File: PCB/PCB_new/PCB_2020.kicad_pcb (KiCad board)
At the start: 2 copper layers, 102.2 x 94.5 mm, 28 parts, among them IC1 LM358N, Q1 220mA/50V/3.5Ω, Q2 100V/17A, Q3 100V/17A, Q4 100V/17A, Q5 100V/17A, Q6 100V/17A, U1 TI_CONN

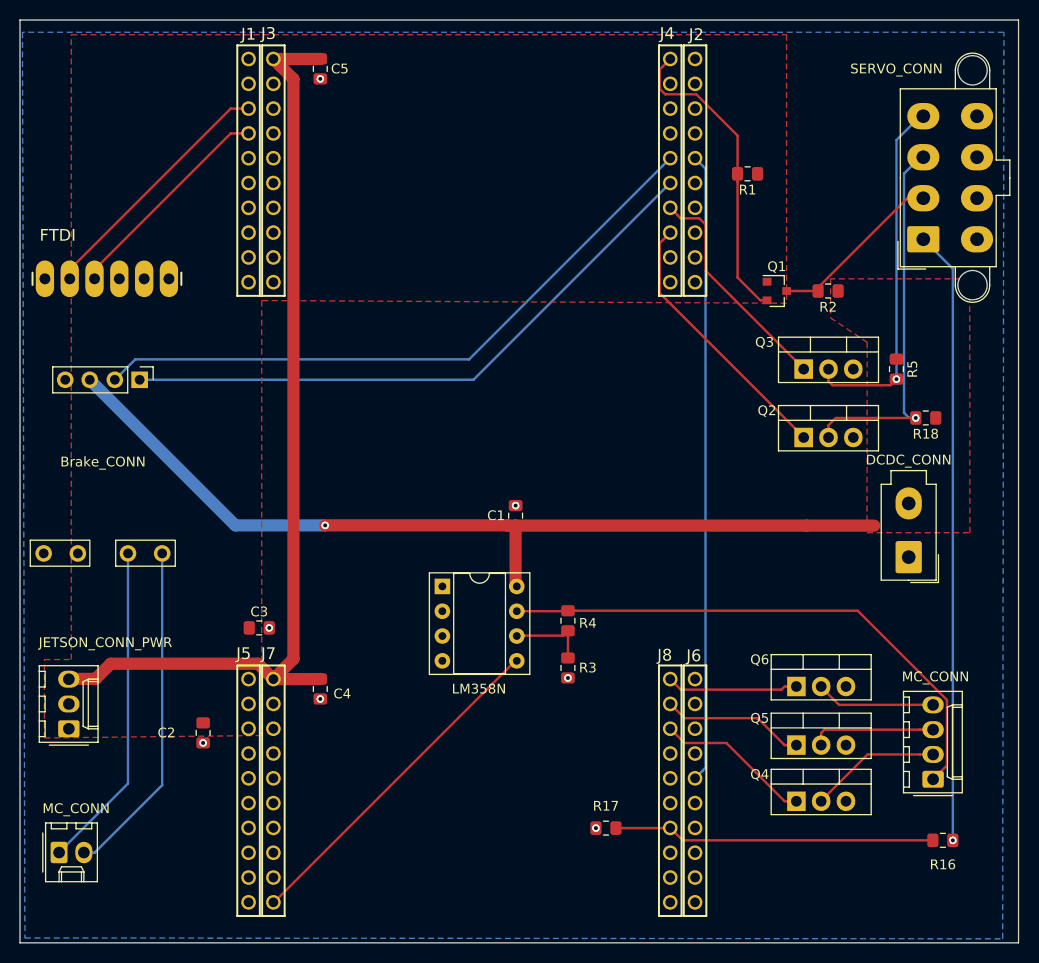
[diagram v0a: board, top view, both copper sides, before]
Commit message: fixed connector notation error
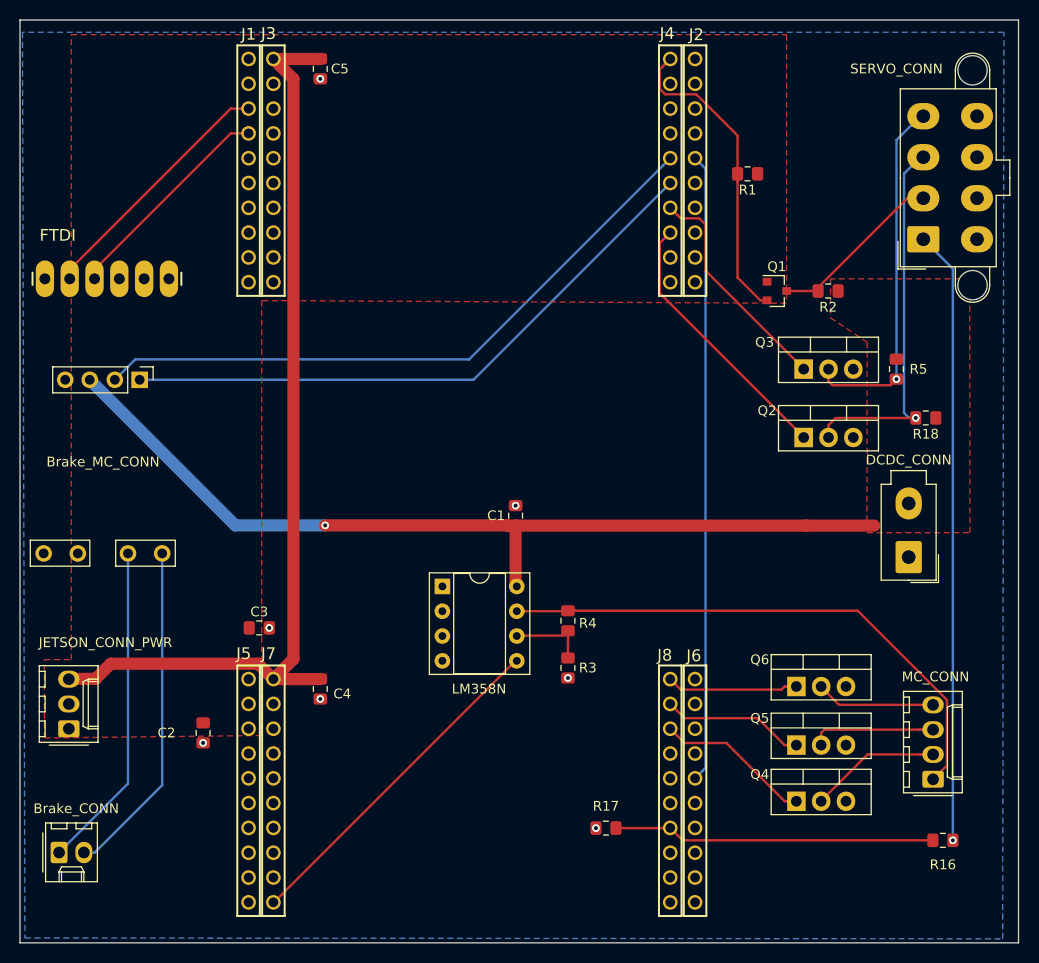
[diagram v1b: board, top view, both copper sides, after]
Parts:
- CONN6: value Brake_CONN -> Brake_MC_CONN
- CONN7: value MC_CONN -> Brake_CONN
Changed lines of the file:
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@@
     (add_net Brake_PWM_2)
     (add_net EN+_CTL)
-    (add_net FEATHER_RESET)
     (add_net FS1_CTL)
     (add_net FWD_CTL)
     (add_net GND)
-    (add_net I2CSCLB)
-    (add_net I2CSDAB)
     (add_net INPUT_A+_CTL)
-    (add_net KILL_SIGNAL)
     (add_net MC_HLFB+)
     (add_net "Net-(CONN1-Pad1)")
     (add_net "Net-(CONN1-Pad5)")
     (add_net "Net-(IC1-Pad6)")
+    (add_net "Net-(U1-Pad42)")
+    (add_net "Net-(U1-Pad45)")
+    (add_net "Net-(U1-Pad49)")
+    (add_net "Net-(U1-Pad50)")
     (add_net "Net-(U1-Pad75)")
     (add_net "Net-(U1-Pad76)")
@@
       (effects (font (size 1 1) (thickness 0.15)))
     )
-    (fp_text value MC_CONN (at 1.75 -4.5) (layer F.SilkS)
+    (fp_text value Brake_CONN (at 1.75 -4.5) (layer F.SilkS)
       (effects (font (size 1 1) (thickness 0.15)))
     )
@@
       (effects (font (size 1 1) (thickness 0.15)))
     )
-    (fp_text value Brake_CONN (at 0 1) (layer F.SilkS)
+    (fp_text value Brake_MC_CONN (at 0 1) (layer F.SilkS)
       (effects (font (size 1 1) (thickness 0.15)))
     )
@@
     (tags "resistor handsolder")
     (attr smd)
-    (fp_text reference R5 (at 0 -1.65 90) (layer F.SilkS)
-      (effects (font (size 1 1) (thickness 0.15)))
-    )
+    (fp_text reference R5 (at 0 -2.25 180) (layer F.SilkS)
+      (effects (font (size 1 1) (thickness 0.15)))
+    )

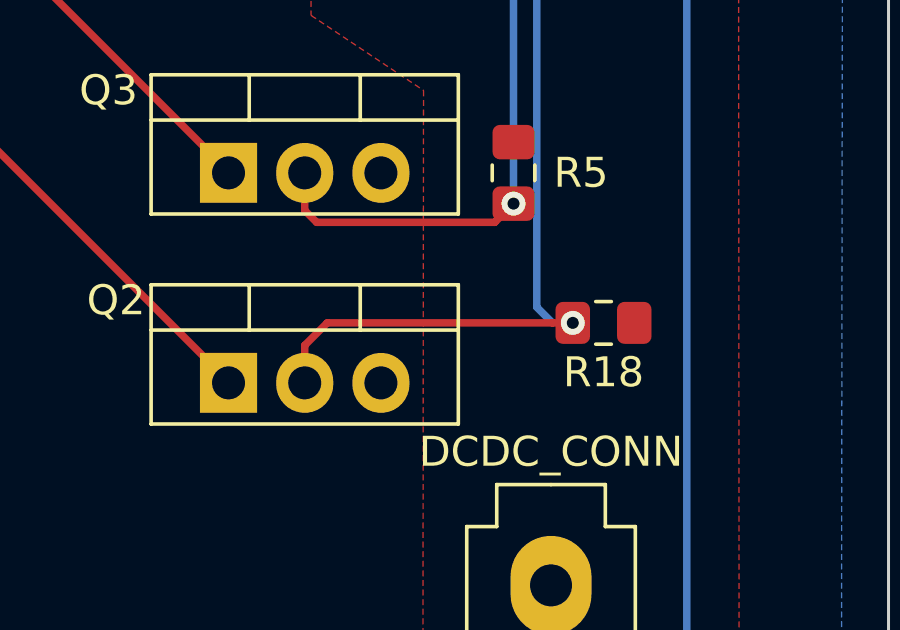
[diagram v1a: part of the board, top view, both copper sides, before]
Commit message: fixed drc connection issue
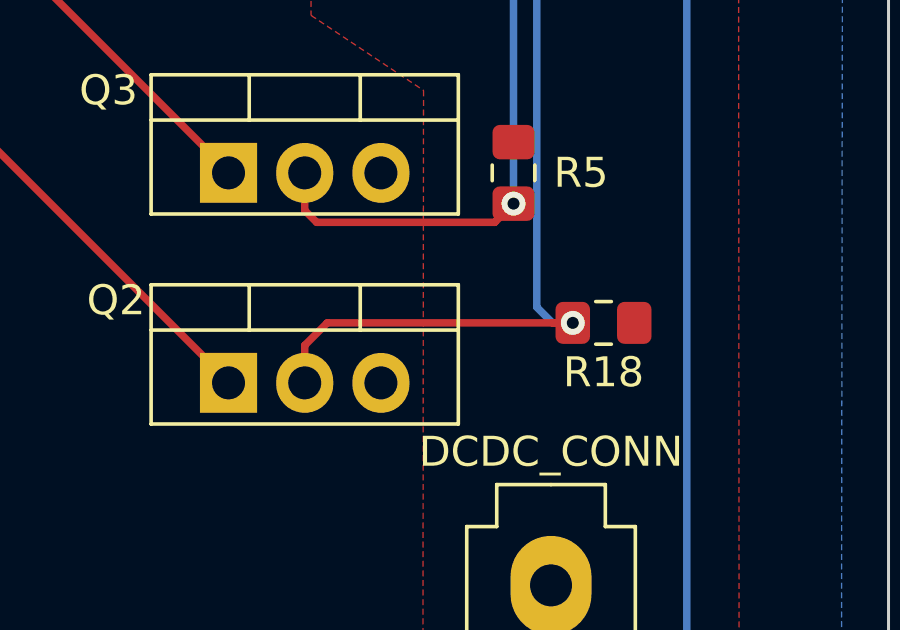
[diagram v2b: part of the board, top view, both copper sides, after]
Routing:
- net /LAUNCHXL-F28379D Breakout/INPUT_A+: track 38.4 -> 39.8 mm
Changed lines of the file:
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@@
     (thickness 1.6)
     (drawings 1)
-    (tracks 142)
+    (tracks 143)
     (zones 0)
     (modules 28)
@@
     (add_net "/LAUNCHXL-F28379D Breakout/REV_MC")
     (add_net "/LAUNCHXL-F28379D Breakout/THROTTLE_MC")
-    (add_net "/LAUNCHXL-F28379D Headers/ADCA0")
-    (add_net "/LAUNCHXL-F28379D Headers/ADCIN1")
-    (add_net "/LAUNCHXL-F28379D Headers/ADCIN15")
-    (add_net "/LAUNCHXL-F28379D Headers/ADCINA2")
-    (add_net "/LAUNCHXL-F28379D Headers/ADCINA3")
-    (add_net "/LAUNCHXL-F28379D Headers/ADCINA4")
-    (add_net "/LAUNCHXL-F28379D Headers/ADCINA5")
-    (add_net "/LAUNCHXL-F28379D Headers/ADCINB2")
-    (add_net "/LAUNCHXL-F28379D Headers/ADCINB3")
-    (add_net "/LAUNCHXL-F28379D Headers/ADCINB4")
-    (add_net "/LAUNCHXL-F28379D Headers/ADCINB5")
-    (add_net "/LAUNCHXL-F28379D Headers/ADCINC2")
-    (add_net "/LAUNCHXL-F28379D Headers/ADCINC3")
-    (add_net "/LAUNCHXL-F28379D Headers/ADCINC4")
-    (add_net "/LAUNCHXL-F28379D Headers/ADCINC5")
-    (add_net "/LAUNCHXL-F28379D Headers/GPIO1-PWMOUT1B")
-    (add_net "/LAUNCHXL-F28379D Headers/GPIO104-I2CSDAA-J1")
-    (add_net "/LAUNCHXL-F28379D Headers/GPIO105-I2SSCLA-J1")
-    (add_net "/LAUNCHXL-F28379D Headers/GPIO111")
-    (add_net "/LAUNCHXL-F28379D Headers/GPIO122-SD1D1")
-    (add_net "/LAUNCHXL-F28379D Headers/GPIO123-SD1CLK1")
-    (add_net "/LAUNCHXL-F28379D Headers/GPIO124-SD1D2")
-    (add_net "/LAUNCHXL-F28379D Headers/GPIO125-SD1CLK2")
-    (add_net "/LAUNCHXL-F28379D Headers/GPIO130-SD2D1")
-    (add_net "/LAUNCHXL-F28379D Headers/GPIO131-SD2CLK1")
-    (add_net "/LAUNCHXL-F28379D Headers/GPIO139-SCICRX(->MCU)")
-    (add_net "/LAUNCHXL-F28379D Headers/GPIO15-OPXBAR4")
-    (add_net "/LAUNCHXL-F28379D Headers/GPIO2-PWMOUT2A")
-    (add_net "/LAUNCHXL-F28379D Headers/GPIO22")
-    (add_net "/LAUNCHXL-F28379D Headers/GPIO25-OPXBAR2")
-    (add_net "/LAUNCHXL-F28379D Headers/GPIO26-SD2D2")
-    (add_net "/LAUNCHXL-F28379D Headers/GPIO27-SD2CLK2")
-    (add_net "/LAUNCHXL-F28379D Headers/GPIO29-OPXBAR6")
-    (add_net "/LAUNCHXL-F28379D Headers/GPIO3-PWMOUT2B")
-    (add_net "/LAUNCHXL-F28379D Headers/GPIO32")
-    (add_net "/LAUNCHXL-F28379D Headers/GPIO52-J5")
-    (add_net "/LAUNCHXL-F28379D Headers/GPIO56-SCICTX(<-MCU)")
-    (add_net "/LAUNCHXL-F28379D Headers/GPIO58-SPIAMOSI")
-    (add_net "/LAUNCHXL-F28379D Headers/GPIO59-SPIAMISO")
-    (add_net "/LAUNCHXL-F28379D Headers/GPIO60-SPICLKA")
-    (add_net "/LAUNCHXL-F28379D Headers/GPIO61-SPIACS")
-    (add_net "/LAUNCHXL-F28379D Headers/GPIO63-SPIBMOSI")
-    (add_net "/LAUNCHXL-F28379D Headers/GPIO64-SPIBMISO")
-    (add_net "/LAUNCHXL-F28379D Headers/GPIO65-SPIBCLK")
-    (add_net "/LAUNCHXL-F28379D Headers/GPIO66-SPIBCS")
-    (add_net "/LAUNCHXL-F28379D Headers/GPIO67")
-    (add_net "/LAUNCHXL-F28379D Headers/GPIO94")
-    (add_net "/LAUNCHXL-F28379D Headers/PWM-BASED-DAC1")
-    (add_net "/LAUNCHXL-F28379D Headers/PWM-BASED-DAC2")
-    (add_net "/LAUNCHXL-F28379D Headers/PWM-BASED-DAC3")
-    (add_net "/LAUNCHXL-F28379D Headers/PWM-BASED-DAC4")
     (add_net "/LAUNCHXL-F28379D Headers/RESET")
     (add_net Brake_PWM_1)
@@
     (add_net INPUT_A+_CTL)
     (add_net MC_HLFB+)
-    (add_net "Net-(CONN1-Pad1)")
-    (add_net "Net-(CONN1-Pad5)")
     (add_net "Net-(IC1-Pad6)")
-    (add_net "Net-(U1-Pad42)")
-    (add_net "Net-(U1-Pad45)")
-    (add_net "Net-(U1-Pad49)")
-    (add_net "Net-(U1-Pad50)")
-    (add_net "Net-(U1-Pad75)")
-    (add_net "Net-(U1-Pad76)")
-    (add_net "Net-(U1-Pad77)")
     (add_net REV_CTL)
     (add_net SCIB_RX)
@@
   (segment (start 178.54 89.5) (end 178.54 88.25) (width 0.25) (layer Top) (net 18))
   (segment (start 178.54 88.25) (end 179.29 87.5) (width 0.25) (layer Top) (net 18))
-  (segment (start 179.29 87.5) (end 186.8 87.5) (width 0.25) (layer Top) (net 18))
   (via (at 187.475 87.5) (size 0.8) (drill 0.4) (layers Top Bottom) (net 18))
   (segment (start 186.27499 62.47501) (end 187.95 60.8) (width 0.25) (layer Bottom) (net 18))
   (segment (start 186.27499 86.97499) (end 186.27499 62.47501) (width 0.25) (layer Bottom) (net 18))
-  (segment (start 186.8 87.5) (end 186.27499 86.97499) (width 0.25) (layer Bottom) (net 18))
   (segment (start 187.95 60.8) (end 188.25 60.8) (width 0.25) (layer Bottom) (net 18))
+  (segment (start 179.29 87.5) (end 187.475 87.5) (width 0.25) (layer Top) (net 18))
+  (segment (start 186.8 87.5) (end 187.475 87.5) (width 0.25) (layer Bottom) (net 18))
+  (segment (start 186.27499 86.97499) (end 186.8 87.5) (width 0.25) (layer Bottom) (net 18))
   (segment (start 186.78 64.838) (end 177.475 74.143) (width 0.25) (layer Top) (net 19))
   (segment (start 174.35 74.5) (end 177.475 74.5) (width 0.25) (layer Top) (net 19))

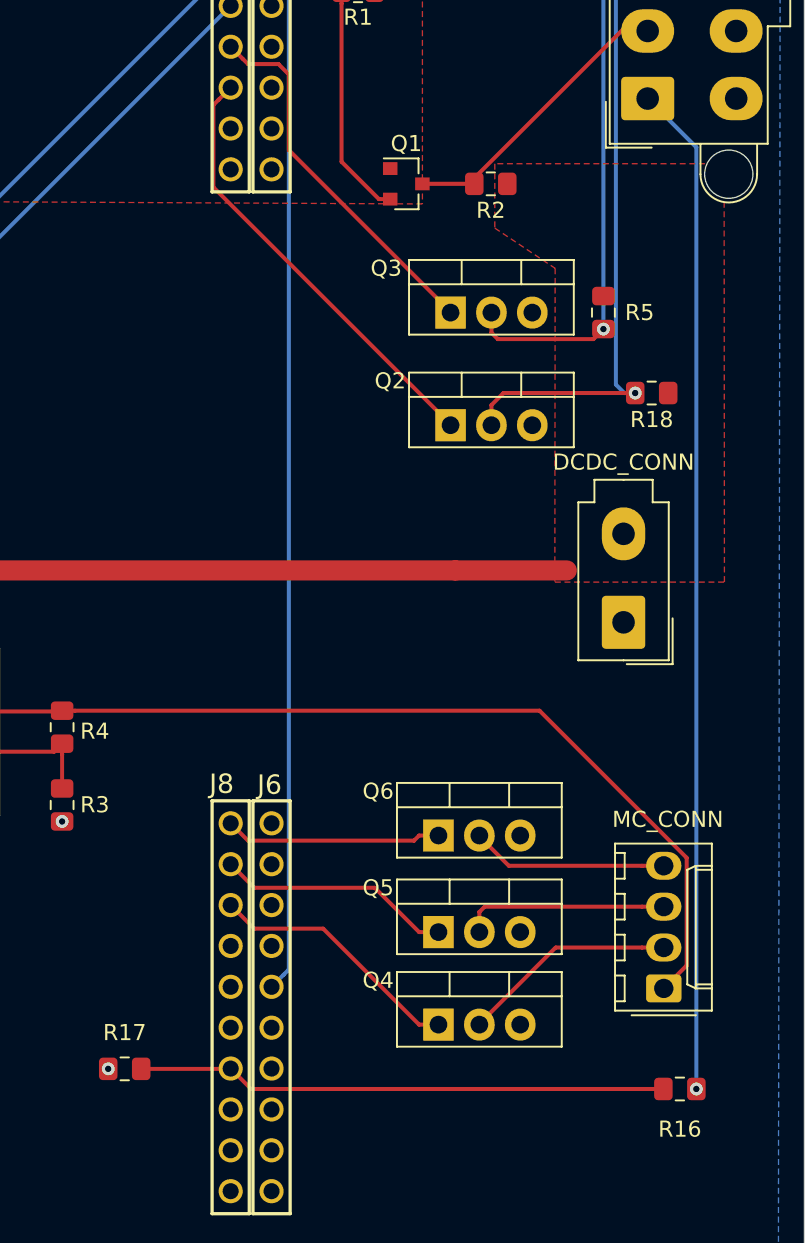
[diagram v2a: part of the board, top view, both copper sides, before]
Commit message: removed signals to HLFB+ for steering motor
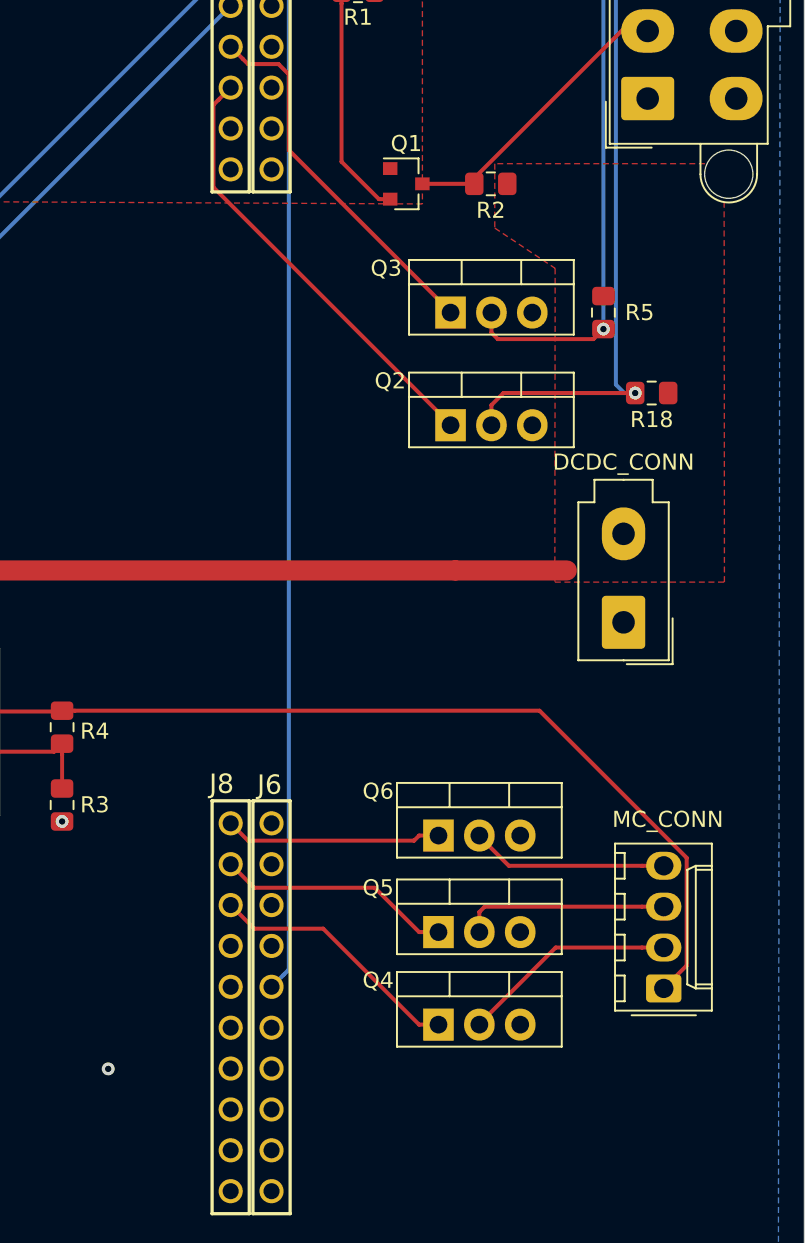
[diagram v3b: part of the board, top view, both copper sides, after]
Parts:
- removed R16, R17: R-US_R0805, Resistor_SMD:R_0805_2012Metric_Pad1.15x1.40mm_HandSolder
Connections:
- CONN2 pad 1: /LAUNCHXL-F28379D Breakout/HLFB+ -> GND
- U1 pad 74: MC_HLFB+ -> (no net)
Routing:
- net /LAUNCHXL-F28379D Breakout/HLFB+: track 62.8 -> 0.00 mm, vias 1 -> 0
- net MC_HLFB+: track 33.0 -> 0.00 mm
